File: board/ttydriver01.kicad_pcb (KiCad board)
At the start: 2 copper layers, 119.4 x 74.9 mm, 59 parts, among them J1 PRINTER JACK, J2 KEYBOARD JACK, J3 MOTOR CTL RELAY JACK, M1 narrower_0.3mm, M2 narrower_0.3mm, M3 narrower_0.3mm, M4 narrower_0.3mm, M5 narrower_0.3mm, M7 narrower_0.3mm, P1 CONN_01X02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

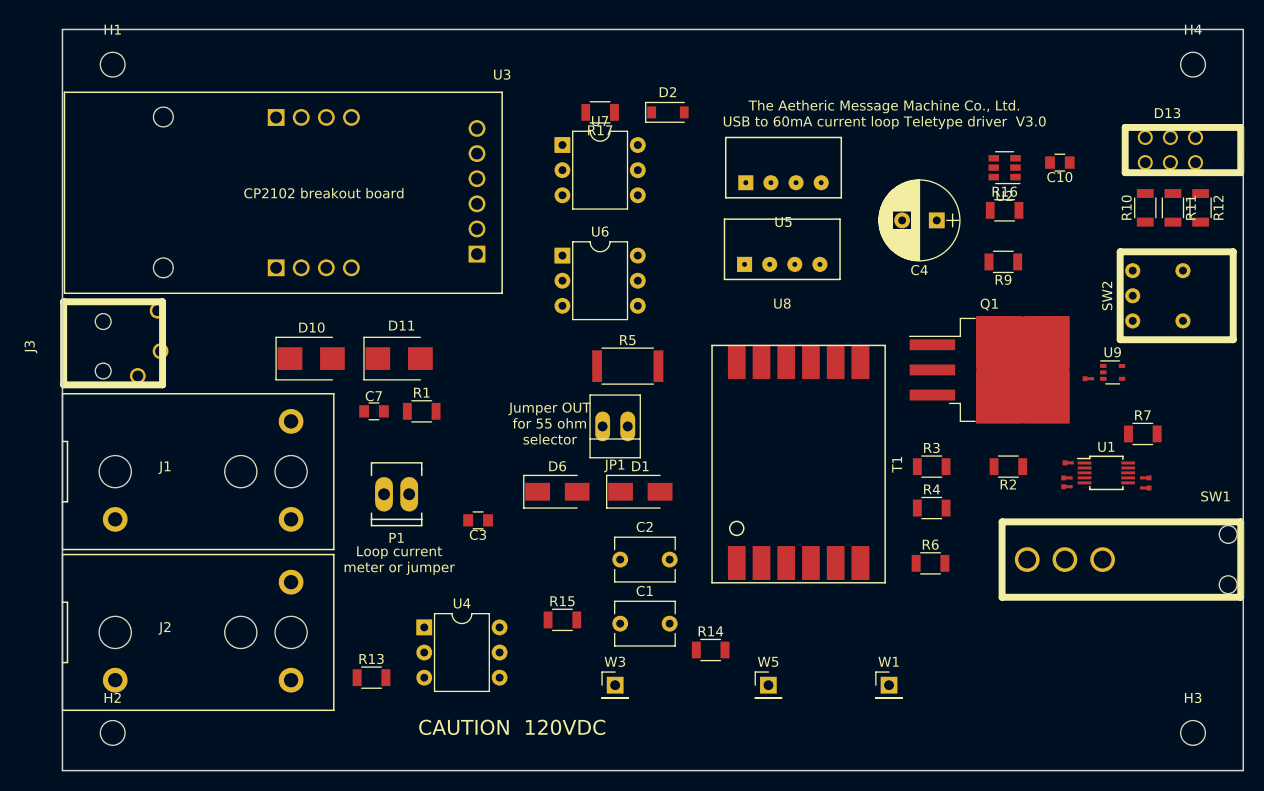
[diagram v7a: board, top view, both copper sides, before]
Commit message: Switch optos to SMD form
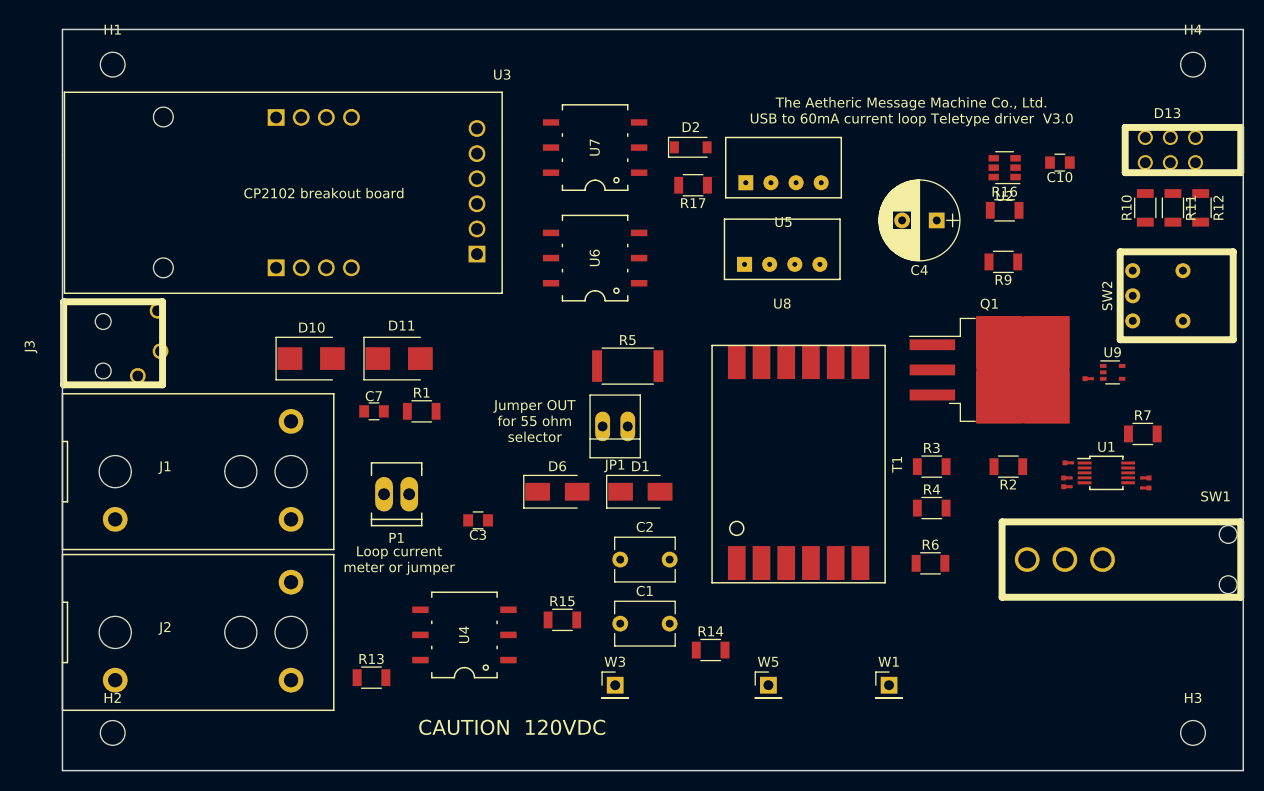
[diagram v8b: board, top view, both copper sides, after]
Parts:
- U4, U6, U7: footprint Housings_DIP:DIP-6_W7.62mm -> SMD_Misc:SMD-6
- moved R17 11.9 mm to (119.6, 93.2)
- moved D2 4.22 mm to (119.4, 89.4)
- moved U4 4.13 mm to (96.5, 138.7), turned to 90 degrees
- moved U6 3.31 mm to (109.7, 100.6), turned to 90 degrees
- moved U7 3.31 mm to (109.7, 89.4), turned to 90 degrees
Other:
- net class Default: clearance 0.25 -> 0.245
- net class Thin: clearance 0.2 -> 0.19
- rule trace_clearance: 0.25 -> 0.245
